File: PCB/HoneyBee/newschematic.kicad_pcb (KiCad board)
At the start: 2 copper layers, 42 parts, among them J1 S2B-PH-K-SLFSN, J2 10104110-0001LF, M1 Motor_DC, M2 Motor_DC, M3 Motor_DC, M4 Motor_DC, M5 Motor_DC, M6 Motor_DC, Q1 IRLML2502TRPbF, Q2 IRLML2502TRPbF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

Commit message: Small updates
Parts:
- moved Q2 68.2 mm to (211.7, 97.5)
- moved U1 62.2 mm to (224.8, 57.3)
- moved U2 57.9 mm to (205.5, 47.0)
- moved CR3 50.6 mm to (224.3, 85.5)
- moved R3 47.9 mm to (210.6, 72.0)
- moved M1 45.4 mm to (176.4, 91.0)
- moved J2 44.9 mm to (189.8, 105.2)
- moved U3 28.8 mm to (176.3, 42.5)
- moved U6 25.0 mm to (198.2, 86.8)
- moved CR1 19.4 mm to (155.2, 79.5)
- moved CR2 19.4 mm to (155.2, 82.0)
- moved U8 16.2 mm to (160.0, 102.2)
- moved J1 13.7 mm to (182.5, 57.0)

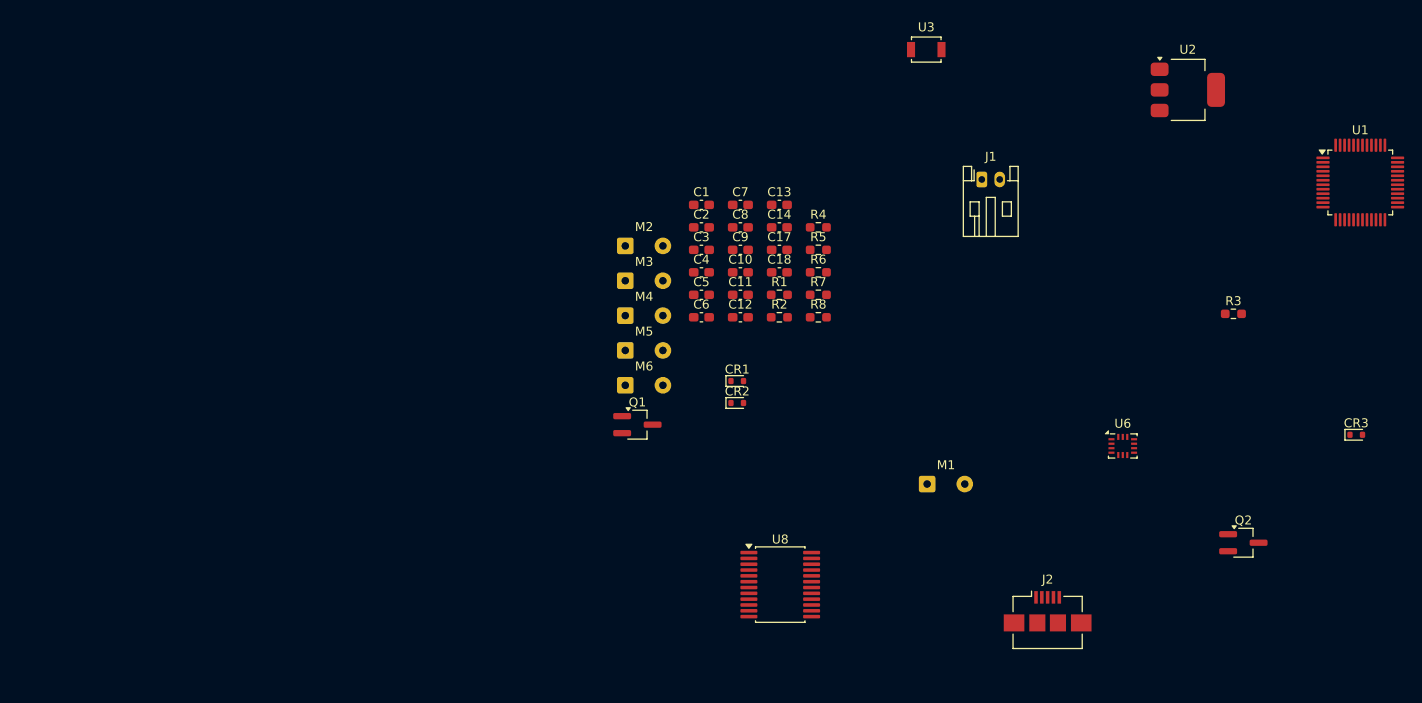
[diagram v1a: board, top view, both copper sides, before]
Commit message: Updated BOM, Changed Components
Added "Price" and "DigiKey" to BOM
Changed out of stock components and non-Cut Reel components.
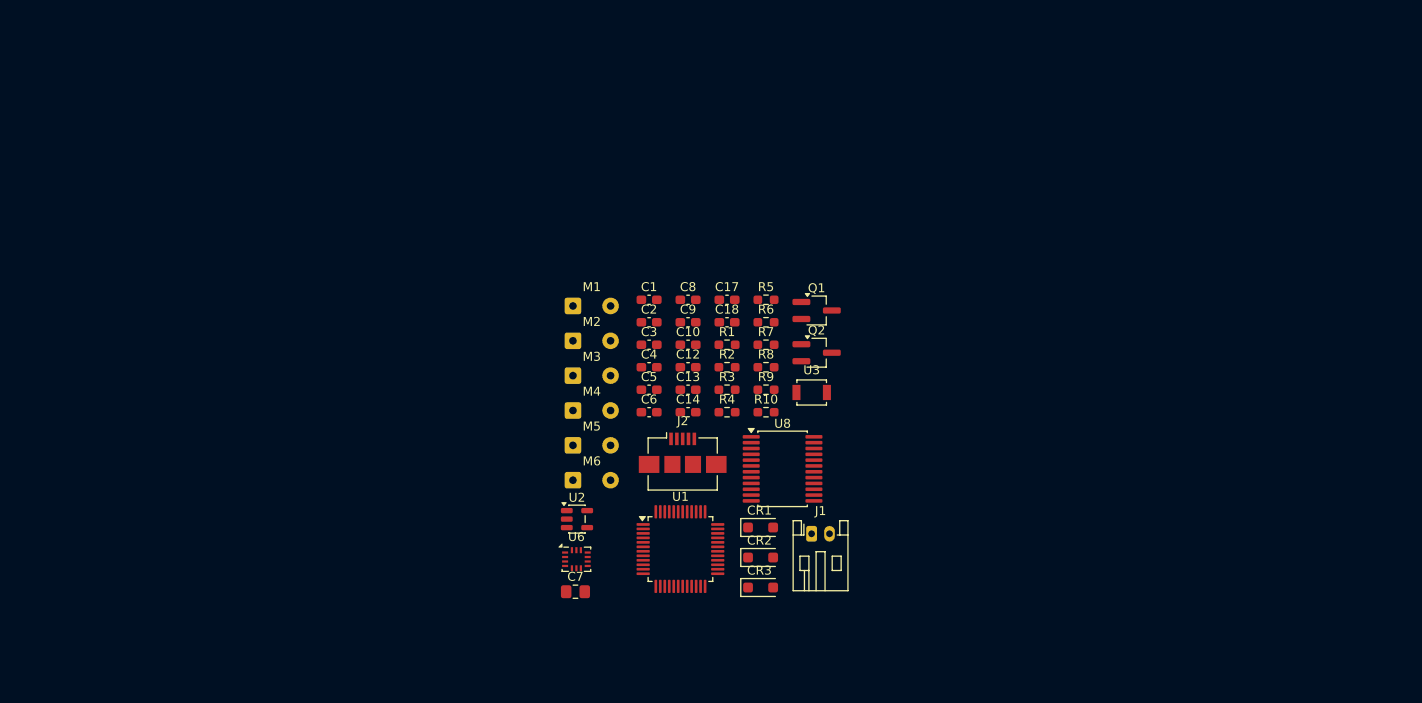
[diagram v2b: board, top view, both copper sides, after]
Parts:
- removed C11: 10 uF, Capacitor_SMD:C_0603_1608Metric_Pad1.08x0.95mm_HandSolder
- added R10: 52.3K, Resistor_SMD:R_0603_1608Metric_Pad0.98x0.95mm_HandSolder, F.Cu at (158.4, 83.0)
- added R9: 30.1K, Resistor_SMD:R_0603_1608Metric_Pad0.98x0.95mm_HandSolder, F.Cu at (158.4, 80.5)
- C7: footprint Capacitor_SMD:C_0603_1608Metric_Pad1.08x0.95mm_HandSolder -> Capacitor_SMD:C_0805_2012Metric_Pad1.18x1.45mm_HandSolder
- CR1, CR2, CR3: value PMEG2010AEB -> SS24FL; footprint Diode_SMD:D_SOD-523 -> Diode_SMD:D_SOD-123F
- U2: value LM2940HS-3.3 -> TPS73733DCQR; footprint Package_TO_SOT_SMD:SOT-223-3_TabPin2 -> Package_TO_SOT_SMD:SOT-23-5
- moved U1 86.2 mm to (148.9, 98.3)
- moved U2 83.3 mm to (137.3, 94.9)
- moved CR3 68.6 mm to (157.8, 102.5)
- moved U6 62.3 mm to (137.2, 99.4)
- moved R3 57.2 mm to (154.1, 80.5)
- moved Q2 52.1 mm to (164.1, 76.3)
- moved C7 46.9 mm to (137.1, 103.0)
- moved J2 44.4 mm to (149.1, 87.5)
- moved M1 44.3 mm to (136.9, 71.1)
- moved J1 43.9 mm to (163.5, 96.5)
- moved U3 40.4 mm to (163.5, 80.8)
- moved Q1 23.7 mm to (164.1, 71.6)
- moved C14 23.0 mm to (149.7, 83.0)
- moved R4 23.0 mm to (154.1, 83.0)
- moved C13 23.0 mm to (149.7, 80.5)
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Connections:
- U2 pad 1: GND -> Net-(M1-+)
- U2 pad 2: +3.3V -> GND

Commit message: Small Tweaks
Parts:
- U2: footprint Package_TO_SOT_SMD:SOT-23-5 -> Package_TO_SOT_SMD:SOT-223-6_TabPin3
- moved Q1 56.4 mm to (117.0, 102.7)
- moved Q2 56.4 mm to (117.0, 107.4)
- moved J1 27.3 mm to (142.4, 79.2)
- moved U3 22.6 mm to (142.3, 88.7)
- moved C10 22.6 mm to (128.5, 83.2)
- moved C12 22.6 mm to (128.5, 85.7)
- moved C13 22.6 mm to (128.5, 88.2)
- moved C14 22.6 mm to (128.5, 90.7)
- moved C18 22.6 mm to (132.9, 80.6)
- moved C2 22.6 mm to (124.2, 80.6)
- moved C3 22.6 mm to (124.2, 83.2)
- moved C4 22.6 mm to (124.2, 85.7)
- moved C5 22.6 mm to (124.2, 88.2)
- moved C6 22.6 mm to (124.2, 90.7)
- moved C9 22.6 mm to (128.5, 80.6)
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
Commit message: Update newschematic.kicad_pcb
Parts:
- moved Q2 77.3 mm to (189.9, 81.5), turned to 45 degrees
- moved M1 76.5 mm to (192.2, 76.6), turned to 135 degrees
- moved M6 71.2 mm to (186.8, 99.8), turned to -135 degrees
- moved C1 69.6 mm to (193.8, 78.6), turned to -135 degrees
- moved Q1 69.6 mm to (182.8, 80.1), turned to 45 degrees
- moved M4 66.7 mm to (181.6, 100.6), turned to 45 degrees
- moved M2 65.7 mm to (181.2, 86.4), turned to 45 degrees
- moved C5 64.8 mm to (188.8, 92.1), turned to -90 degrees
- moved M3 62.5 mm to (177.0, 98.8), turned to -90 degrees
- moved C14 58.9 mm to (187.2, 95.8), turned to -45 degrees
- moved CR1 57.0 mm to (187.0, 77.0), turned to 135 degrees
- moved CR3 55.3 mm to (186.2, 85.8), turned to -135 degrees
- moved R2 55.1 mm to (187.8, 89.4), turned to -135 degrees
- moved C3 54.7 mm to (177.5, 95.2)
- moved C17 54.3 mm to (180.0, 105.1), turned to -157.5 degrees
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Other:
- board outline added: 42.4 x 42.4 mm

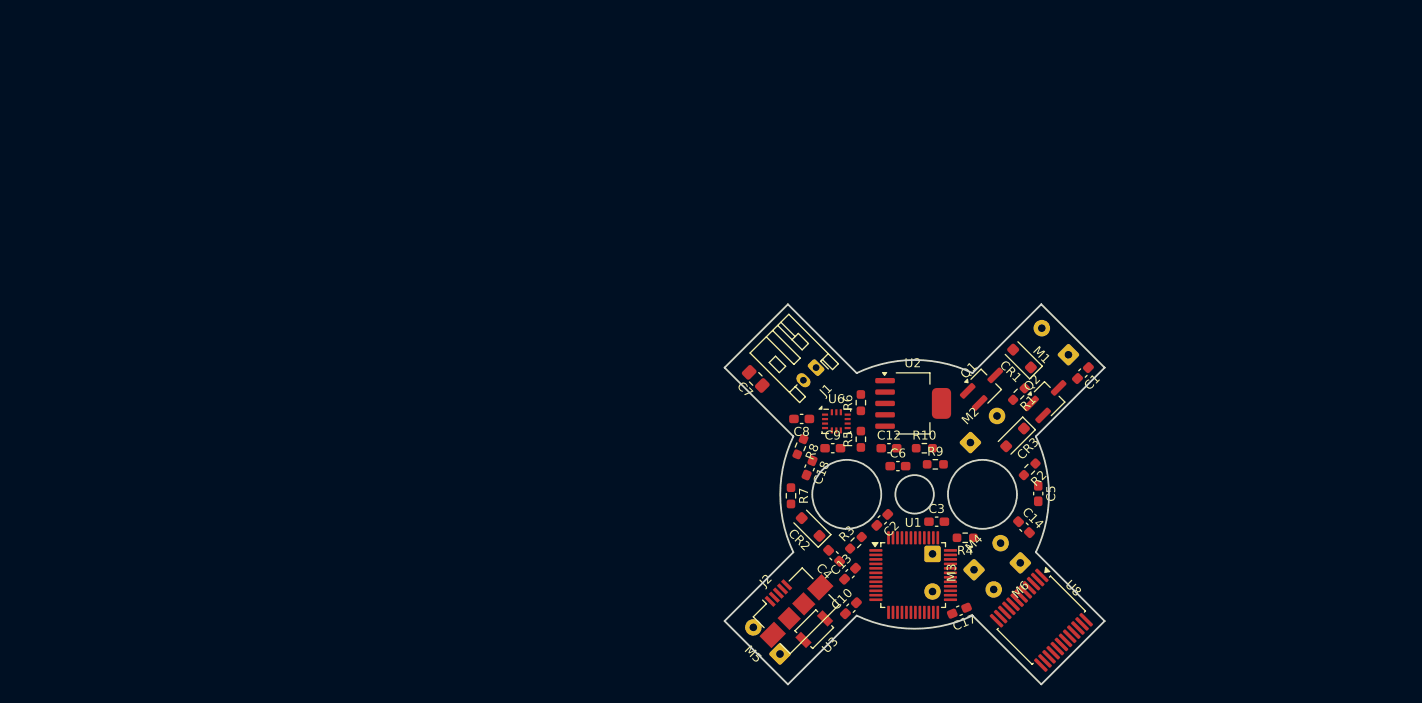
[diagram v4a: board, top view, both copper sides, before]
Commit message: PCB Draft 1-Minimal Wiring
Still adjusting location of components.
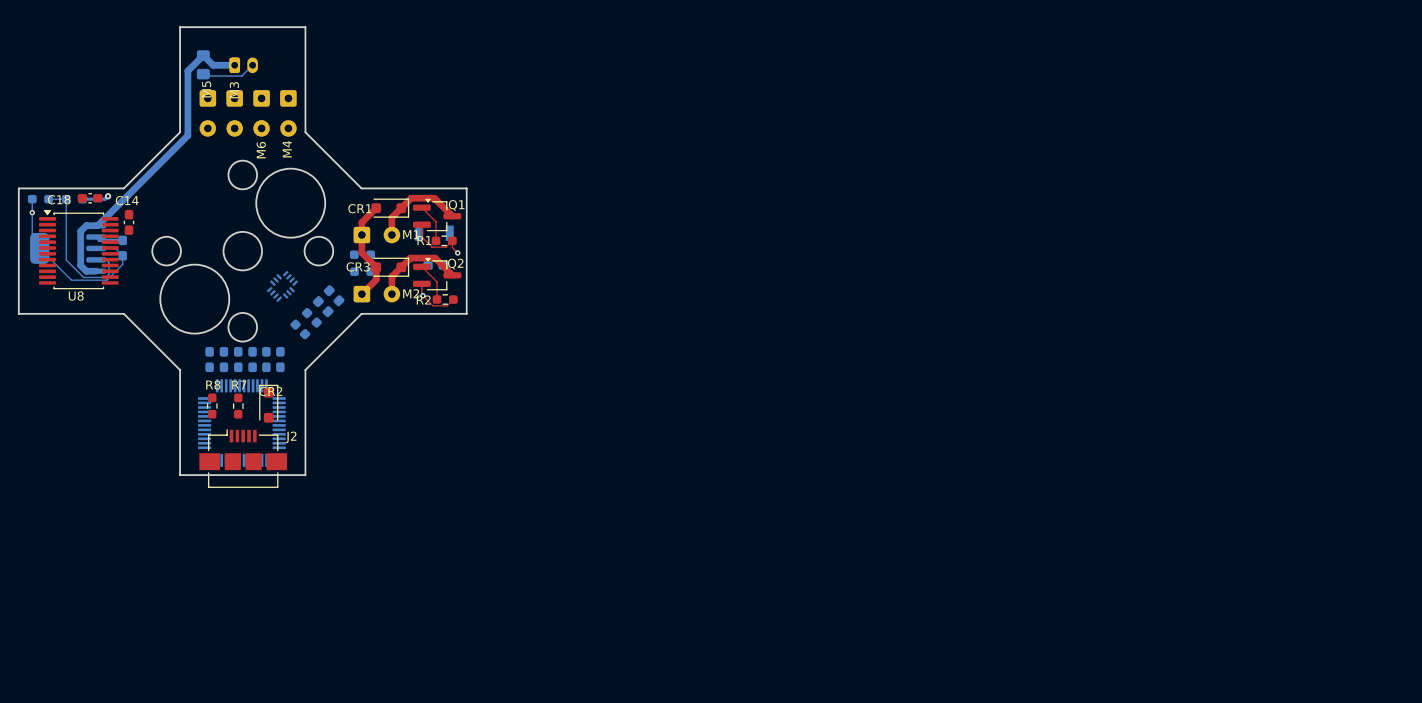
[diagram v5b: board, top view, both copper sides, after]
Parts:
- removed C1, C5: 0.1 uF, Capacitor_SMD:C_0603_1608Metric_Pad1.08x0.95mm_HandSolder
- C10, C12, C13, C17, C2, C3, C4, C6, C7, C8, C9, J1, R10, R3, R4, R5, R6, R9, U1, U2, U3, U6: moved to B.Cu
- moved U8 115.1 mm to (81.7, 65.0), turned to 0 degrees
- moved C14 105.5 mm to (87.3, 61.8), turned to 90 degrees
- moved R9 104.2 mm to (77.4, 59.2), turned to 180 degrees
- moved R10 98.9 mm to (81.2, 59.2), turned to 180 degrees
- moved M6 98.8 mm to (102.1, 49.0), turned to -90 degrees
- moved U2 95.9 mm to (80.5, 64.7), turned to 180 degrees
- moved M3 92.5 mm to (99.1, 49.0)
- moved M4 92.3 mm to (105.1, 49.0), turned to -90 degrees
- moved C12 88.4 mm to (86.6, 64.7), turned to 90 degrees
- moved M5 88.3 mm to (96.1, 49.0), turned to -90 degrees
- moved C17 86.8 mm to (97.9, 77.1), turned to 90 degrees
- moved C18 85.8 mm to (83.0, 59.1), turned to 180 degrees
- moved M1 79.0 mm to (114.3, 63.2), turned to 0 degrees
- moved C6 77.8 mm to (96.3, 77.1), turned to 90 degrees
- moved C3 77.0 mm to (102.6, 77.1), turned to 90 degrees
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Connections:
- Q1 pad 1: Net-(M1--) -> Net-(Q1-G)
- Q1 pad 2: Net-(Q1-G) -> GND
- Q1 pad 3: GND -> Net-(M1--)
- Q2 pad 1: Net-(M2--) -> Net-(Q2-G)
- Q2 pad 2: Net-(Q2-G) -> GND
- Q2 pad 3: GND -> Net-(M2--)
- U2 pad 2: GND -> +3.3V
- U2 pad 3: Net-(M1-+) -> GND
- U2 pad 5: +3.3V -> Net-(M1-+)
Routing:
- net Net-(M1-+): track 0.00 -> 47.4 mm
- net GND: track 0.00 -> 40.4 mm, vias 0 -> 3
- net Net-(U2-NR): track 0.00 -> 17.3 mm
- net Net-(M1--): track 0.00 -> 10.4 mm
- net Net-(M2--): track 0.00 -> 10.4 mm
- net +3.3V: track 0.00 -> 6.09 mm, vias 0 -> 1
- net Net-(Q1-G): track 0.00 -> 4.35 mm
- net Net-(Q2-G): track 0.00 -> 4.35 mm
- added copper zone on In2.Cu, net +3.3V
- added copper zone on In1.Cu, net GND
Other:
- board size 42.4 x 42.4 mm -> 50 x 50 mm
- copper layers 2 -> 4
